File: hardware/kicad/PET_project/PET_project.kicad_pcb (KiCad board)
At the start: 2 copper layers, 106 x 40 mm, 25 parts, among them J1 Conn_01x02_Socket, J2 Screw_Terminal_01x02, J3 Screw_Terminal_01x02, J4 Conn_01x02_Socket, J5 GY-GPSV2-NEO6M, J6 BMM350, J7 MPU6050, J8 Conn_01x02_Socket, J9 BMP280, Q2 NMOS, Q3 NMOS, U8 LM317_TO-220

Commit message: board
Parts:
- removed the REF** at (107.5, 107.5)
- removed the REF** at (198.5, 107.5)
- removed the REF** at (107.5, 132.5)
- removed the REF** at (198.5, 132.5)
- added REF**: MountingHole_2.5mm, MountingHole:MountingHole_2.5mm, F.Cu at (104.6, 155.4)
- added REF**: MountingHole_2.5mm, MountingHole:MountingHole_2.5mm, F.Cu at (205.4, 155.4)
- added REF**: MountingHole_2.5mm, MountingHole:MountingHole_2.5mm, F.Cu at (205.4, 104.6)
- added REF**: MountingHole_2.5mm, MountingHole:MountingHole_2.5mm, F.Cu at (104.6, 104.6)
- C1: footprint Capacitor_THT:CP_Radial_Tantal_D5.0mm_P2.50mm -> Capacitor_THT:CP_Radial_Tantal_D4.5mm_P5.00mm
- C2: value 0.33 -> 22; footprint Capacitor_THT:CP_Radial_Tantal_D5.0mm_P2.50mm -> Capacitor_THT:C_Radial_D5.0mm_H11.0mm_P2.00mm
- J5: footprint my_footprint:NEO6M_PinSocket_Vertical -> my_footprint:GY-GPSV2-NEO6M
- U8: value LM317_TO-220 -> BA50DD0T
- moved J3 92.5 mm to (203.6, 143.5)
- moved J2 82.9 mm to (204.4, 122.4)
- moved Q3 80.7 mm to (194.6, 143.5), turned to -90 degrees
- moved R5 75.7 mm to (191.6, 146.2), turned to -90 degrees
- moved J4 75.6 mm to (114.8, 107.9), turned to 180 degrees
- moved R4 69.7 mm to (191.1, 126.7), turned to -90 degrees
- moved Q2 69.6 mm to (194.6, 123.5), turned to -90 degrees
- moved R7 67.5 mm to (188.8, 143.5), turned to 0 degrees
- moved R3 61.8 mm to (188.3, 123.5), turned to 0 degrees
- moved J1 59.3 mm to (123.8, 107.9), turned to 180 degrees
- moved U1 38.0 mm to (176.2, 111.4), turned to 90 degrees
- moved J6 37.0 mm to (152.0, 133.4), turned to 0 degrees
- moved J7 29.7 mm to (139.5, 134.5), turned to 0 degrees
- moved J9 27.9 mm to (128.0, 128.5), turned to 0 degrees
- moved U2 27.1 mm to (137.5, 113.5), turned to 0 degrees
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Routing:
- net +3V3: track 72.5 -> 142.8 mm, vias 2 -> 0
- net /UART_RX: track 63.7 -> 8.71 mm
- net /I2C1_SDA: track 49.5 -> 100.8 mm, vias 1 -> 0
- net /UART_TX: track 56.3 -> 11.5 mm
- net +5V: track 89.7 -> 45.2 mm, vias 2 -> 0
- net /I2C1_SCL: track 46.6 -> 87.9 mm
- net /nichrome2: track 19.9 -> 40.5 mm
- net +6V: track 67.8 -> 78.5 mm, vias 2 -> 0
- net /SPI_SCK: track 9.73 -> 19.3 mm
- net /SPI_CS: track 26.6 -> 17.9 mm
- net /SPI_MISO: track 12.2 -> 19.3 mm
- net Net-(J3-Pin_1): track 13.6 -> 9.00 mm
- net Net-(J1-Pin_1): track 10.9 -> 7.27 mm
- net Net-(J1-Pin_2): track 14.5 -> 10.8 mm
- net /SPI_MOSI: track 15.8 -> 19.3 mm
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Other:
- board size 106 x 40 mm -> 110 x 60 mm

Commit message: Update PET_project.kicad_pcb
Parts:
- moved J3 3.29 mm to (206.5, 144.8), turned to 180 degrees
- moved J2 2.16 mm to (206.5, 122.0), turned to 180 degrees
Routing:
- net Net-(J3-Pin_1): track 9.00 -> 12.8 mm
- net Net-(J2-Pin_1): track 10.3 -> 12.8 mm

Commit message: borad2
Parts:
- added C3: C, Capacitor_THT:CP_Radial_D6.3mm_P2.50mm, F.Cu at (105.5, 118.5)
- moved J6 33.9 mm to (119.0, 125.8)
- moved J3 24.1 mm to (183.5, 137.9), turned to -90 degrees
- moved R5 21.6 mm to (180.7, 127.5), turned to 180 degrees
- moved R7 19.4 mm to (183.5, 124.8), turned to -90 degrees
- moved J9 19.0 mm to (109.0, 127.3)
- moved J5 18.1 mm to (156.5, 137.5), turned to -90 degrees
- moved Q3 17.0 mm to (183.5, 130.5), turned to 180 degrees
- moved REF** 10.0 mm to (104.6, 145.4)
- moved REF** 10.0 mm to (205.4, 145.4)
- moved J7 9.65 mm to (132.0, 128.4)
- moved R4 3.46 mm to (191.1, 123.3)
- moved J2 3.17 mm to (206.5, 118.8)
- moved R3 2.99 mm to (188.8, 120.5)
- moved J1 2.50 mm to (123.8, 110.4)
- moved J4 2.50 mm to (114.8, 110.4)
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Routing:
- net +6V: track 78.5 -> 111.1 mm
- net /I2C1_SCL: track 87.9 -> 103.8 mm
- net /UART_TX: track 11.5 -> 24.5 mm
- net +3V3: track 142.8 -> 132.2 mm
- net /UART_RX: track 8.71 -> 18.8 mm
- net /nichrome2: track 40.5 -> 31.6 mm
- net GND: track 6.02 -> 0.00 mm, vias 0 -> 138
- net Net-(J3-Pin_1): track 12.8 -> 7.39 mm
- net /I2C1_SDA: track 100.8 -> 105.6 mm, vias 0 -> 1
- net /nichrome1: track 26.8 -> 30.9 mm
- net Net-(J4-Pin_2): track 23.0 -> 20.9 mm
- net /SPI_CS: track 17.9 -> 19.2 mm
- net Net-(J1-Pin_2): track 10.8 -> 9.79 mm
- net Net-(J4-Pin_1): track 18.4 -> 17.3 mm
- net Net-(J1-Pin_1): track 7.27 -> 6.24 mm
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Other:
- board size 110 x 60 mm -> 110 x 50 mm

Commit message: Update PET_project.kicad_pcb
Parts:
- moved Q2 7.67 mm to (194.6, 129.2)
- moved R3 7.67 mm to (188.8, 128.2)
- moved J2 7.67 mm to (206.5, 126.5)
- moved R4 7.67 mm to (191.1, 131.0)
- moved C2 6.07 mm to (194.0, 120.0)
- moved C1 5.64 mm to (197.0, 109.5)
- moved J8 5.64 mm to (192.0, 110.5)
- moved U8 5.64 mm to (189.5, 116.0)
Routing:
- net +5V: track 45.2 -> 56.6 mm
- net /nichrome1: track 30.9 -> 38.6 mm
- net +6V: track 111.1 -> 114.4 mm
- net GND: track 0.00 -> 2.12 mm, vias 138 -> 191

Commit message: borad
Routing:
- net /I2C1_SDA: track 105.6 -> 108.5 mm
- net /I2C1_SCL: track 103.8 -> 105.8 mm
- net GND: vias 191 -> 196

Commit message: 基板設計変更②
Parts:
- removed J1, J4: Conn_01x02_Socket, Connector_JST:JST_XH_S2B-XH-A_1x02_P2.50mm_Horizontal
- removed U7: ~, my_footprint:XIAO-ESP32-S3-DIP
- removed U8: BA50DD0T, Package_TO_SOT_THT:TO-220-3_Vertical
- added D1: LED, LED_THT:LED_D5.0mm_Clear, F.Cu at (120.8, 144.5)
- added J10: Conn_01x06_Socket, Connector_JST:JST_XH_S6B-XH-A-1_1x06_P2.50mm_Horizontal, F.Cu at (167.5, 103.5)
- added R1: 10k, Resistor_THT:R_Axial_DIN0204_L3.6mm_D1.6mm_P2.54mm_Vertical, F.Cu at (127.2, 146.5)
- added R2: 330, Resistor_THT:R_Axial_DIN0204_L3.6mm_D1.6mm_P2.54mm_Vertical, F.Cu at (112.3, 144.5)
- added U3: MCP23008-xP, Package_DIP:DIP-18_W7.62mm, F.Cu at (107.8, 137.6)
- added U4: BA50DD0T, Package_TO_SOT_THT:TO-220-3_Vertical, F.Cu at (166.0, 116.0)
- J6: value BMM350 -> Conn_01x06_Socket; footprint my_footprint:BMM350_PinSocket_Vertical -> Connector_JST:JST_XH_S6B-XH-A-1_1x06_P2.50mm_Horizontal
- moved R4 58.3 mm to (134.7, 116.0), turned to 180 degrees
- moved J2 57.8 mm to (149.0, 120.5), turned to 90 degrees
- moved R3 57.0 mm to (132.3, 120.5)
- moved Q2 55.7 mm to (139.5, 120.5), turned to 90 degrees
- moved R7 50.7 mm to (133.0, 129.8)
- moved R5 48.8 mm to (133.0, 137.5), turned to 90 degrees
- moved J3 43.3 mm to (140.5, 132.6), turned to 90 degrees
- moved C1 41.9 mm to (155.5, 115.0)
- moved Q3 41.1 mm to (143.0, 137.6)
- moved J7 34.5 mm to (162.5, 144.6), turned to 180 degrees
- moved J8 32.4 mm to (160.0, 105.5)
- moved J6 30.0 mm to (139.0, 103.5)
- moved J9 27.7 mm to (131.5, 143.5), turned to 90 degrees
- moved J5 27.6 mm to (184.0, 135.8)
- moved C3 27.4 mm to (130.8, 108.0)
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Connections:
- J2 pad 2: GND -> +6V
- J3 pad 2: GND -> +6V
- J6 pad 1: unconnected-(J6-Pin_1-Pad1) -> Net-(J6-Pin_1)
- J6 pad 2: unconnected-(J6-Pin_2-Pad2) -> +3V3
- J6 pad 3: unconnected-(J6-Pin_3-Pad3) -> /encoder_LA
- J6 pad 4: unconnected-(J6-Pin_4-Pad4) -> /encoder_LB
- J6 pad 5: unconnected-(J6-Pin_5-Pad5) -> GND
- J6 pad 6: /I2C1_SDA -> Net-(J6-Pin_6)
- U1 pad 1: /SPI_CS -> /encoder_RB
- U1 pad 10: /SPI_MISO -> /pwm_A
- U1 pad 11: /SPI_MOSI -> /pwm_B
- U1 pad 2: /nichrome1 -> /encoder_RA
- U1 pad 3: unconnected-(U1-Pad3) -> /encoder_LA
- U1 pad 4: /nichrome2 -> /encoder_LB
- U1 pad 9: /SPI_SCK -> /RESET
- U2 pad 10: Net-(U2-PWMB) -> /pwm_B
- U2 pad 16: Net-(U2-PWMA) -> /pwm_A
- U2 pad 2: +3V8 -> +3V3
- U2 pad 6: Net-(J4-Pin_1) -> Net-(J6-Pin_1)
- U2 pad 7: Net-(J4-Pin_2) -> Net-(J6-Pin_6)
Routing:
- net +3V3: track 132.2 -> 256.3 mm
- net /RESET: track 0.00 -> 105.6 mm
- net /pwm_B: track 0.00 -> 93.3 mm
- net /pwm_A: track 0.00 -> 80.5 mm
- net /encoder_LA: track 0.00 -> 76.0 mm, vias 0 -> 1
- net /encoder_LB: track 0.00 -> 68.3 mm, vias 0 -> 1
- net Net-(J10-Pin_6): track 9.79 -> 70.6 mm
- net Net-(J10-Pin_1): track 6.24 -> 53.5 mm
- net Net-(J6-Pin_6): track 0.00 -> 42.9 mm
- net +3V8: track 40.1 -> 0.00 mm
- net Net-(U3-GP7): track 0.00 -> 27.9 mm
- net Net-(J6-Pin_1): track 0.00 -> 27.5 mm
- net /nichrome2: track 31.6 -> 5.01 mm
- net /nichrome1: track 38.6 -> 12.3 mm
- net +6V: track 114.4 -> 92.7 mm
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
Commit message: エラー修正
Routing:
- net GND: track 0.00 -> 3.50 mm
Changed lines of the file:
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@@
-	)
-	(segment
-		(start 154.5 108.0925)
-		(end 154.5 108)
-		(width 1)
-		(layer "F.Cu")
-		(net "+6V")
 	)
 	(segment
@@
 	)
 	(segment
+		(start 177.5 103.5)
+		(end 177.5 105.5)
+		(width 1)
+		(layer "F.Cu")
+		(net "GND")
+	)
+	(segment
+		(start 177.5 103.5)
+		(end 177.5 105)
+		(width 1)
+		(layer "B.Cu")
+		(net "GND")
+	)
+	(segment
 		(start 125.52 110)
 		(end 161 110)
@@
 	)
 	(segment
+		(start 139.5 120.5)
+		(end 149 120.5)
+		(width 0.3)
+		(layer "B.Cu")
+		(net "Net-(J2-Pin_1)")
+	)
+	(segment
 		(start 134.72 116)
 		(end 137.54 116)
@@
 	)
 	(segment
-		(start 139.5 120.5)
-		(end 149 120.5)
-		(width 0.3)
-		(layer "B.Cu")
-		(net "Net-(J2-Pin_1)")
-	)
-	(segment

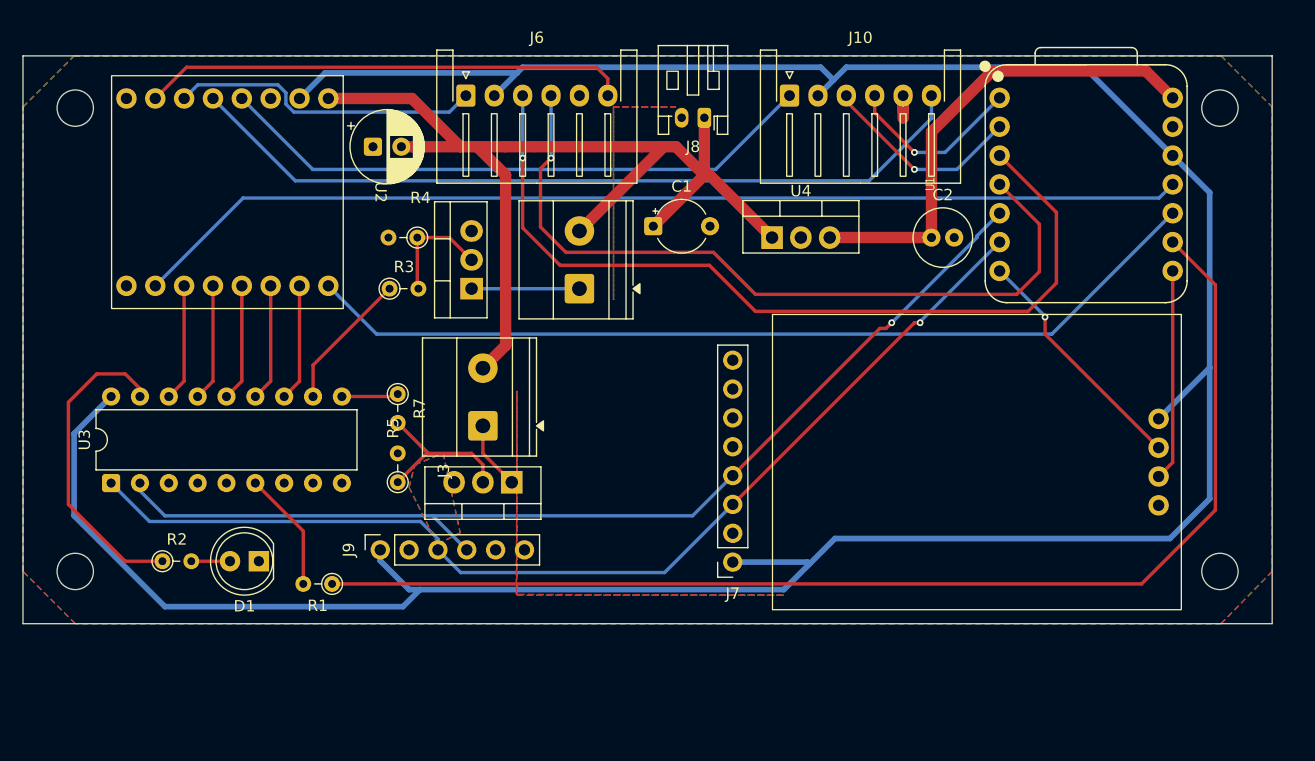
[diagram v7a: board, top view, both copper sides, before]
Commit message: ショットキーバリアダイオード追加
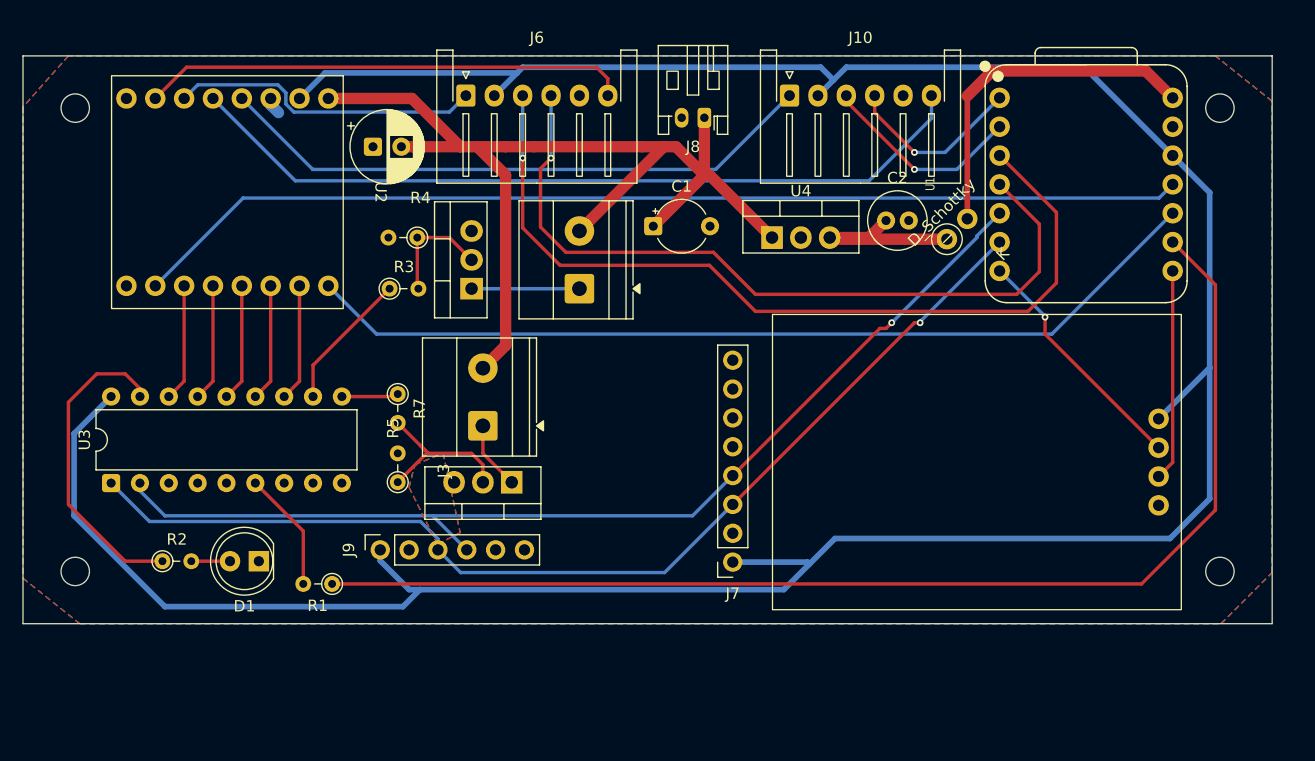
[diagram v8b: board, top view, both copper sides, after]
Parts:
- added D2: D_Schottky, my_footprint:D_schottky, F.Cu at (183.2, 114.3)
- moved C2 4.27 mm to (176.0, 114.5)
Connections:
- U1 pad 14: +5V -> Net-(D2-K)
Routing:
- net Net-(D2-K): track 0.00 -> 30.8 mm
- net +5V: track 42.7 -> 16.0 mm
- net GND: track 3.50 -> 1.54 mm
